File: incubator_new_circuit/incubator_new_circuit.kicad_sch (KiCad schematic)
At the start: 43 parts, among them K1 SANYOU_SRD_Form_C, K2 SANYOU_SRD_Form_C, K3 SANYOU_SRD_Form_C, M1 Fan, Q1 BC547, Q2 BC547, Q3 BC547, SW1 PTH_12x12mm_h8.0mm, SW2 PTH_12x12mm_h8.0mm, SW3 PTH_12x12mm_h8.0mm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

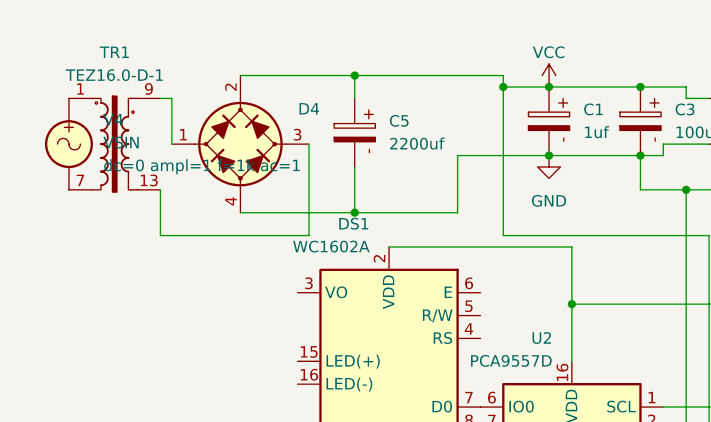
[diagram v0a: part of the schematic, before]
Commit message: chore: Remove unused schematic symbols and associated generated files from the KiCad project.
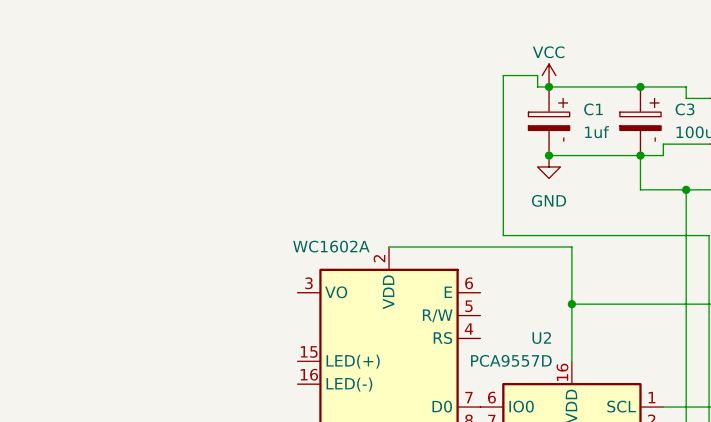
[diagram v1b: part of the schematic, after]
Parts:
- removed C5: 2200uf, Capacitor_THT:CP_Radial_D5.0mm_P2.50mm, symbol PCM_SL_Devices:Capacitor_PO
- removed D4: D_Bridge_Generic_AC+AC-, symbol PCM_Diode_Bridge_AKL:D_Bridge_Generic_AC+AC-
- removed TR1: TEZ16.0-D-1, Transformer_THT:Transformer_Breve_TEZ-47x57, symbol Transformer:TEZ16.0-D-1
- removed V4: VSIN, symbol Simulation_SPICE:VSIN

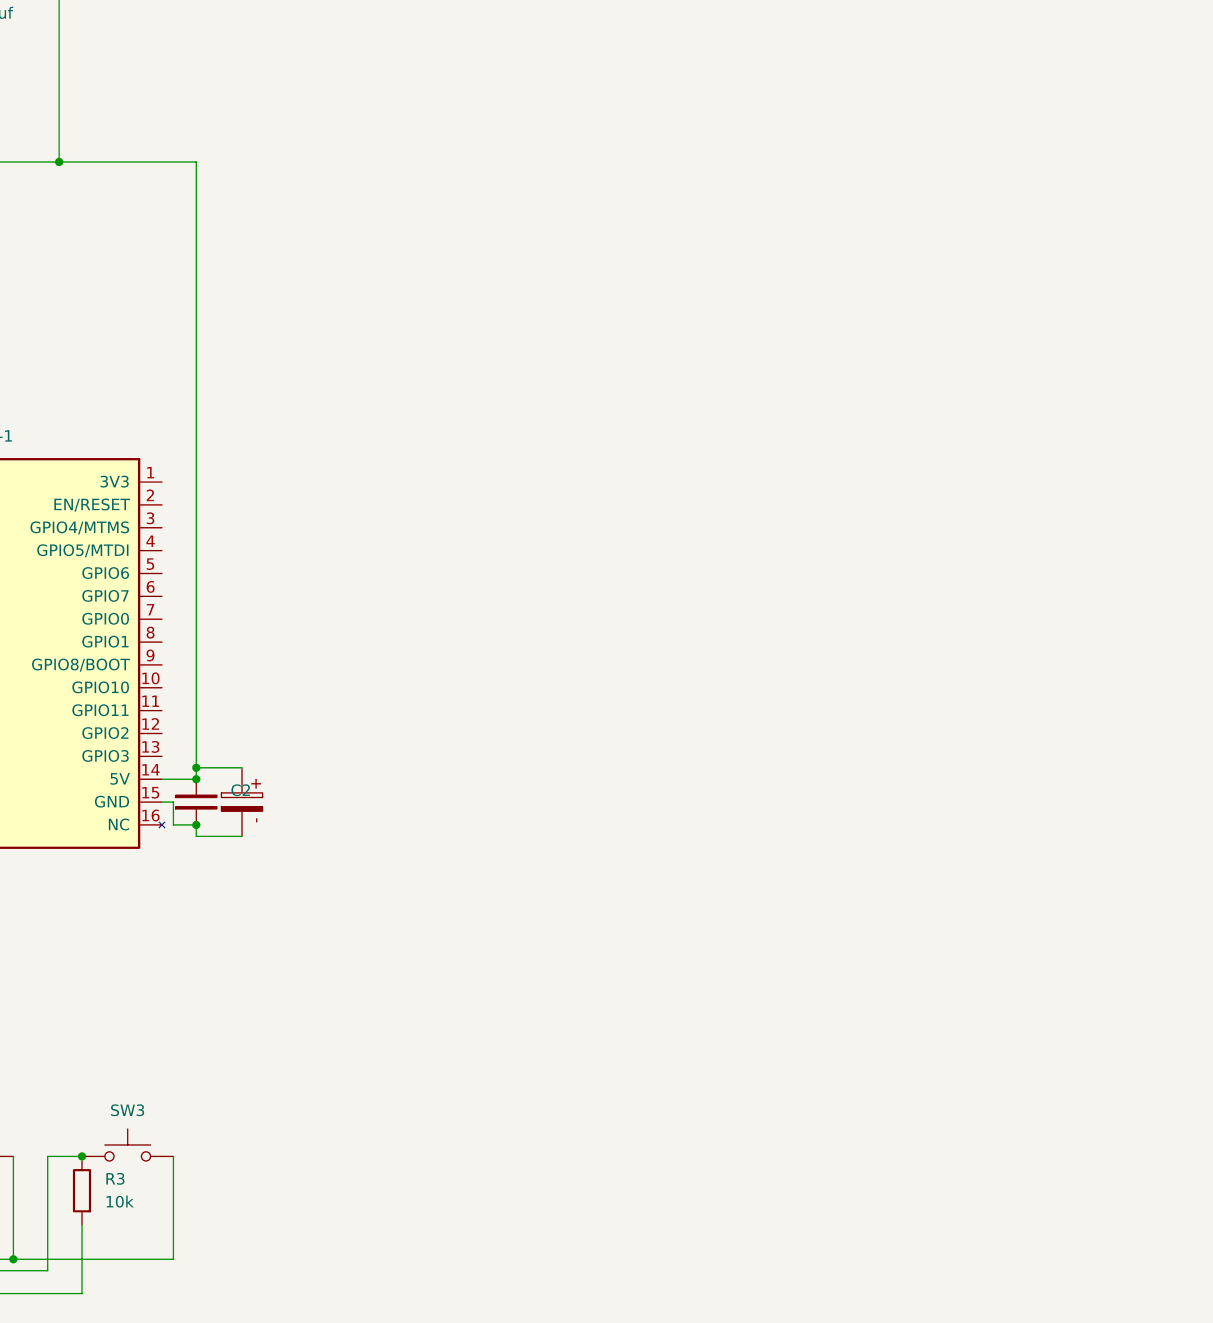
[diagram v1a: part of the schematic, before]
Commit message: feat: Add stepper motor and ULN2003A symbols to the KiCad schematic.
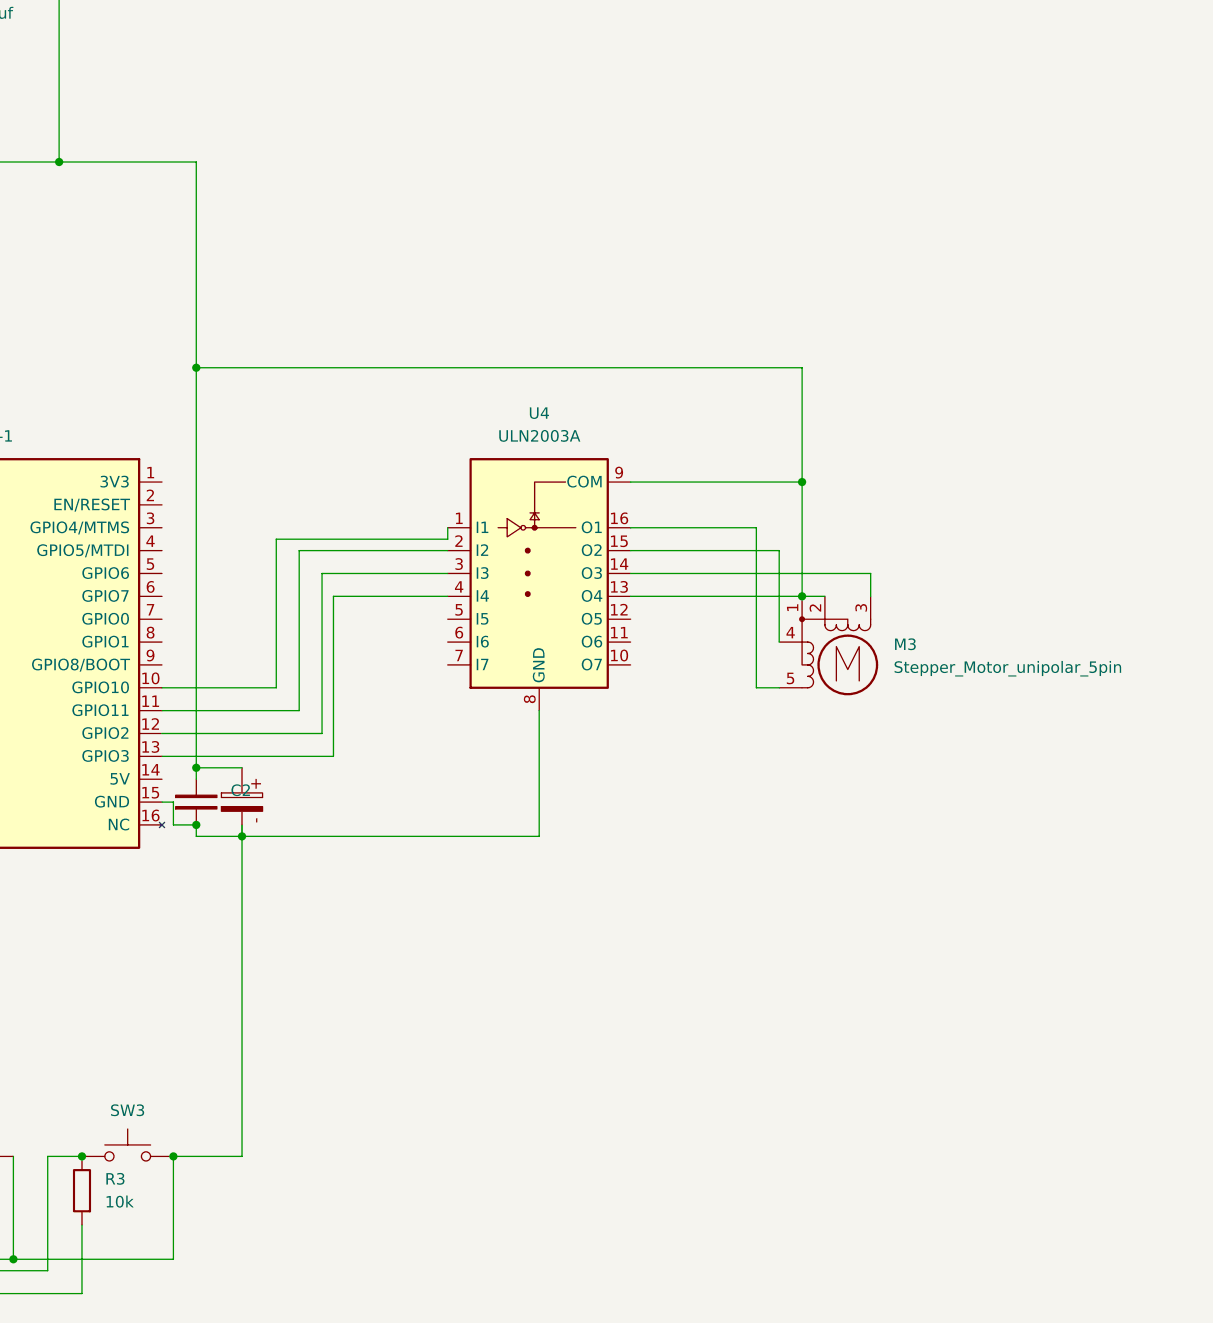
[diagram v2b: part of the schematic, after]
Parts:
- added M3: Stepper_Motor_unipolar_5pin, symbol Motor:Stepper_Motor_unipolar_5pin
- added U4: ULN2003A, symbol Transistor_Array:ULN2003A
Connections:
- net at C17.2, C2.1, U1.15 (GND): now also SW1.2, SW2.2, SW3.2, U4.8 (GND)
- net at C17.1, C2.2, C4.1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: now also M3.1, M3.2, U4.13 (O4), U4.9 (COM); no longer U1.14 (5V)
- net at U1.10 (GPIO10): now also U4.1 (I1)
- net at U1.11 (GPIO11): now also U4.2 (I2)
- net at U1.12 (GPIO2): now also U4.3 (I3)
- net at U1.13 (GPIO3): now also U4.4 (I4)
- new net: M3.3 (-), U4.14 (O3)
- new net: M3.4, U4.15 (O2)
- new net: M3.5, U4.16 (O1)
